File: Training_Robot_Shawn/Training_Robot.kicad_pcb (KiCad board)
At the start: 2 copper layers, 101.5 x 70 mm, 16 parts, among them J1 Arduino connector, J4 3V, J5 GND, M1 FrontL, M2 FrontR, M3 BackL, M4 BackR, SW1 SW_SPDT_312

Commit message: Update contstraints
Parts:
- moved G*** 7.50 mm to (233.0, 92.0)
- moved D1 5.39 mm to (211.0, 88.0)
- moved M1 5.39 mm to (194.5, 82.0)
- moved M2 5.39 mm to (194.5, 58.0)
- moved M3 5.39 mm to (195.5, 95.5)
- moved M4 5.39 mm to (195.5, 71.5)
- moved R1 5.39 mm to (215.4, 80.5)
- moved R2 5.39 mm to (211.0, 96.6)
- moved SW1 5.39 mm to (208.9, 80.5)
- moved U1 5.39 mm to (178.0, 61.8)
- moved U2 5.39 mm to (178.1, 85.6)
- moved U4 5.39 mm to (221.0, 65.5)
- moved J1 5.39 mm to (154.0, 68.0)
- moved J4 2.83 mm to (189.0, 47.5)
- moved J5 2.83 mm to (201.0, 47.5)
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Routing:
- net +3V3: track 176.0 -> 179.0 mm
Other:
- board size 101.5 x 70 mm -> 112.5 x 87 mm
- board text added: "Shawn Mitchell Thanks Jayrady Sok Josalin Wang Austen Yun Carlos Giron"
- board text removed: "Shawn Mitchell Thanks Jayrady Sok Josalin Wang"

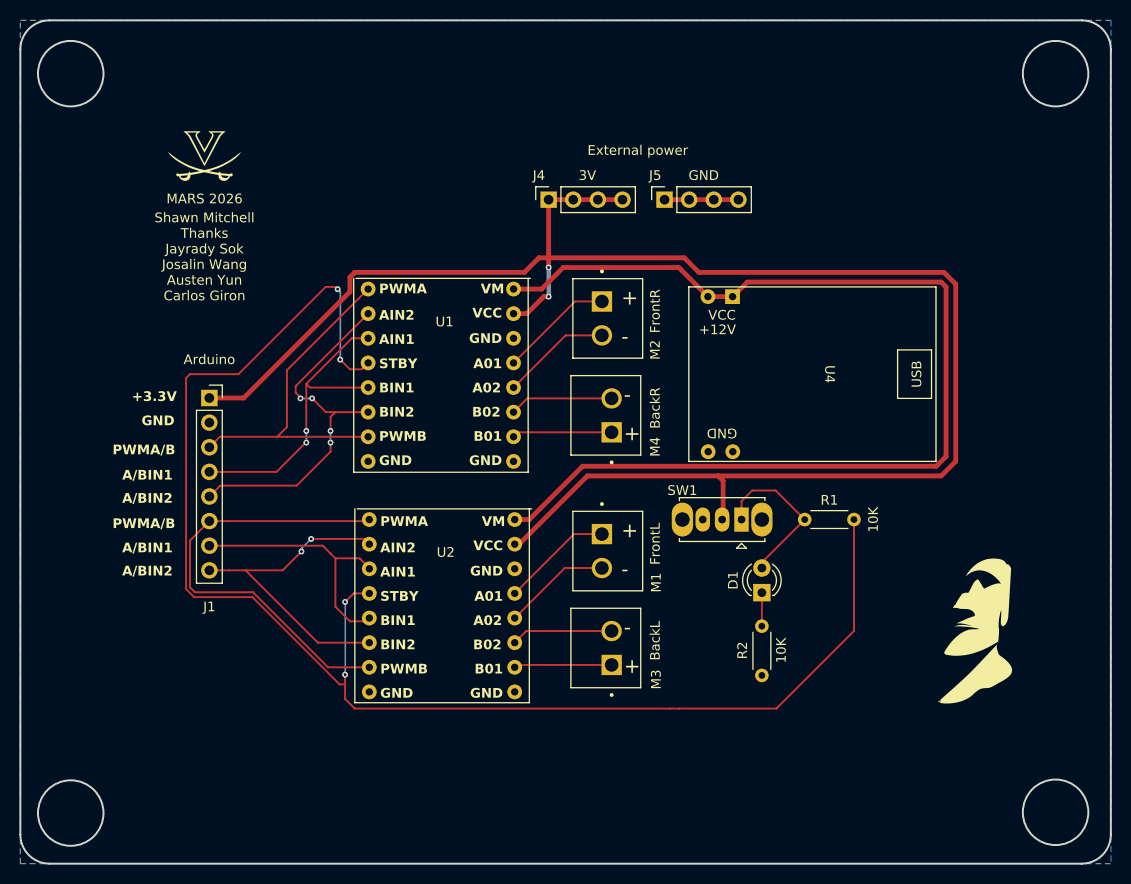
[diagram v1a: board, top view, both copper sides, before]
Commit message: moved a tiny bit
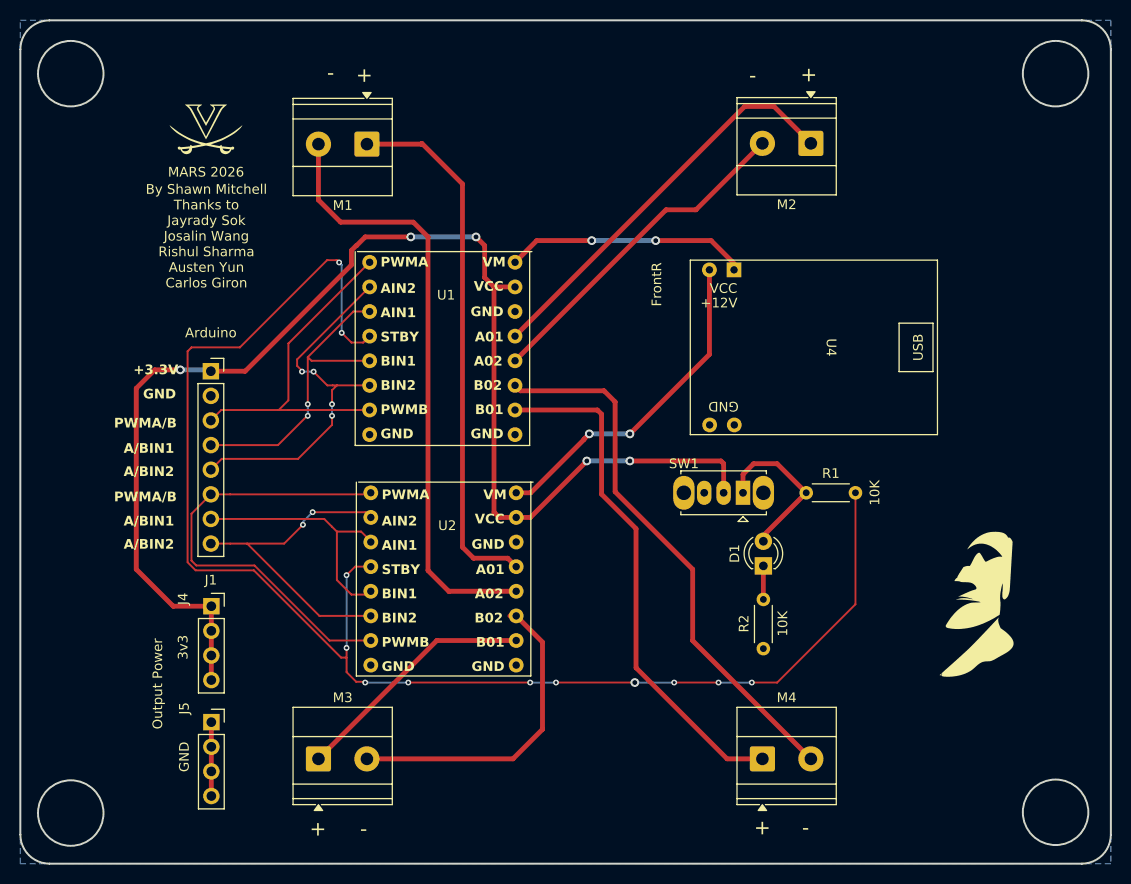
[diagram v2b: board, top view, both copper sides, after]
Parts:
- J4: value 3V -> 3v3
- M1, M2, M3, M4: footprint Library:CUI_TBP03R2-350-02BE -> TerminalBlock_Phoenix:TerminalBlock_Phoenix_MKDS-1,5-2_1x02_P5.00mm_Horizontal
- moved J5 71.4 mm to (154.2, 101.4), turned to 0 degrees
- moved J4 54.5 mm to (154.2, 89.4), turned to 0 degrees
- moved M1 47.0 mm to (170.3, 41.8), turned to 180 degrees
- moved M4 37.1 mm to (211.1, 105.2), turned to 0 degrees
- moved M3 31.8 mm to (165.3, 105.2), turned to 0 degrees
- moved M2 27.0 mm to (216.1, 41.7), turned to 180 degrees
- moved D1 2.77 mm to (211.2, 85.3)
- moved G*** 2.77 mm to (153.7, 40.2)
- moved U4 2.77 mm to (221.1, 62.7)
- moved R1 2.77 mm to (215.6, 77.7)
- moved G*** 2.77 mm to (233.2, 89.2)
- moved J1 2.77 mm to (154.2, 65.2)
- moved R2 2.77 mm to (211.2, 93.8)
- moved SW1 2.77 mm to (209.1, 77.7)
- moved U1 2.77 mm to (178.2, 59.0)
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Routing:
- net +12V motor pwr: track 112.3 -> 59.8 mm, vias 0 -> 4
- net /FL-: track 11.1 -> 63.1 mm
- net /BR-: track 10.7 -> 56.2 mm
- net /BR+: track 10.3 -> 54.3 mm
- net /FL+: track 11.5 -> 55.5 mm
- net +3V3: track 179.0 -> 139.5 mm, vias 2 -> 5
- net /FR+: track 11.7 -> 41.9 mm
- net /FR-: track 11.3 -> 34.8 mm
- net /BL-: track 10.5 -> 32.9 mm
- net /BL+: track 10.1 -> 25.8 mm
- net /STBY: track 153.4 -> 153.6 mm, vias 4 -> 12
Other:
- board text added: "By Shawn Mitchell Thanks to Jayrady Sok Josalin Wang Rishul Sharma Austen Yun Carlos Giron"
- board text added: "Output Power"
- board text removed: "External power"
- board text removed: "M2"
- board text removed: "M4"
- board text removed: "Shawn Mitchell Thanks Jayrady Sok Josalin Wang Austen Yun Carlos Giron"

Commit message: reduced size profile to 3x3 inches between mounting holes (horizontally and vertically)
reduced from 3x4 in between holes
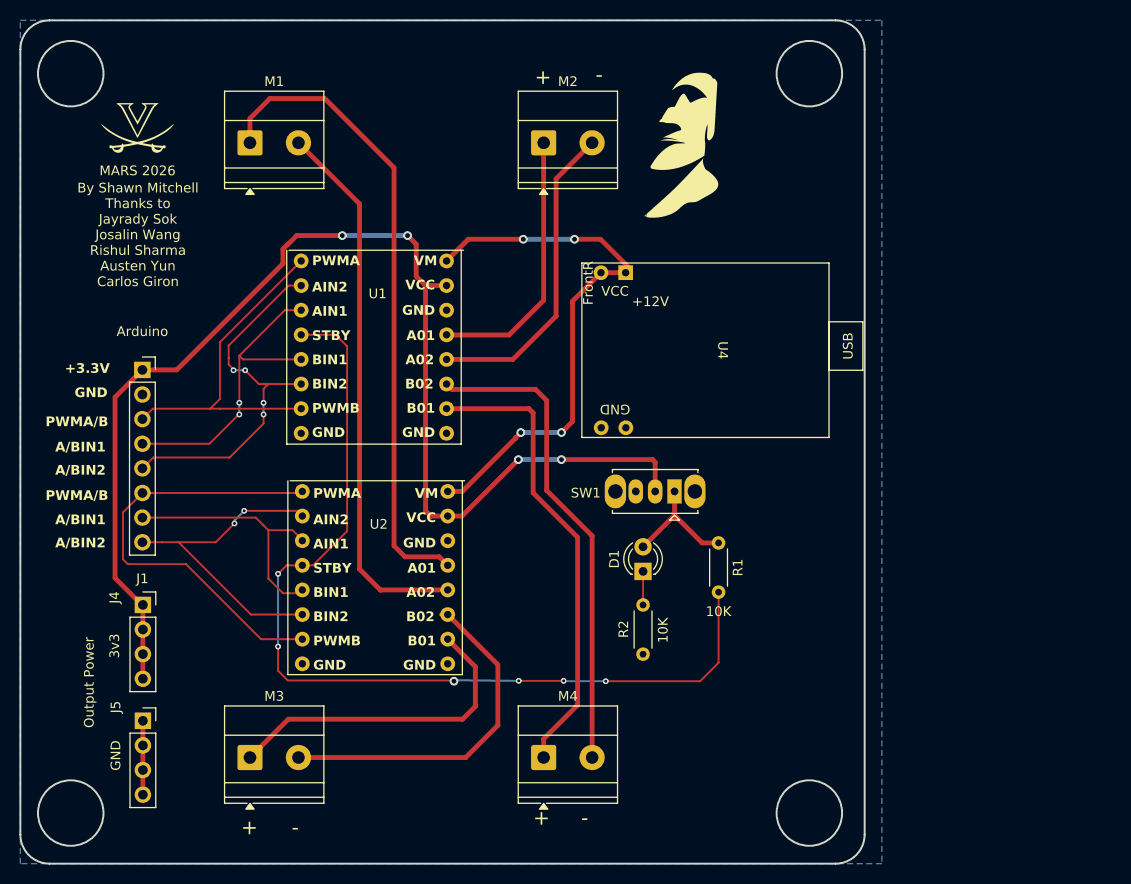
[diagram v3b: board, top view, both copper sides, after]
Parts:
- moved G*** 56.3 mm to (202.7, 41.9)
- moved M2 27.6 mm to (188.5, 41.6), turned to 0 degrees
- moved M4 22.6 mm to (188.5, 105.0)
- moved D1 12.4 mm to (198.7, 85.8)
- moved R2 12.4 mm to (198.7, 94.4)
- moved M1 12.1 mm to (158.2, 41.6), turned to 0 degrees
- moved U4 11.2 mm to (209.9, 63.0)
- moved R1 10.4 mm to (206.5, 82.9), turned to -90 degrees
- moved J4 7.06 mm to (147.1, 89.3)
- moved J5 7.06 mm to (147.1, 101.3)
- moved G*** 7.06 mm to (146.6, 40.1)
- moved J1 7.06 mm to (147.1, 65.1)
- moved M3 7.06 mm to (158.2, 105.0)
- moved SW1 7.06 mm to (202.0, 77.6)
- moved U1 7.06 mm to (171.1, 58.9)
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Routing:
- net /STBY: track 153.6 -> 97.3 mm, vias 12 -> 6
- net /FR+: track 41.9 -> 27.8 mm
- net /FL+: track 55.5 -> 66.5 mm
- net +3V3: track 139.5 -> 129.9 mm, vias 5 -> 4
- net /BL+: track 25.8 -> 33.9 mm
- net /BR-: track 56.2 -> 49.2 mm
- net /FL-: track 63.1 -> 56.6 mm
- net /BR+: track 54.3 -> 48.1 mm
- net Net-(D1-A): track 16.9 -> 12.8 mm
- net /BL-: track 32.9 -> 36.2 mm
- net +12V motor pwr: track 59.8 -> 56.7 mm
- net /FR-: track 34.8 -> 32.6 mm
- net Net-(J1-Pin_5): track 38.3 -> 39.1 mm
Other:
- board size 112.5 x 87 mm -> 87.1 x 87 mm
- board text removed: "M1"
- board text removed: "M3"

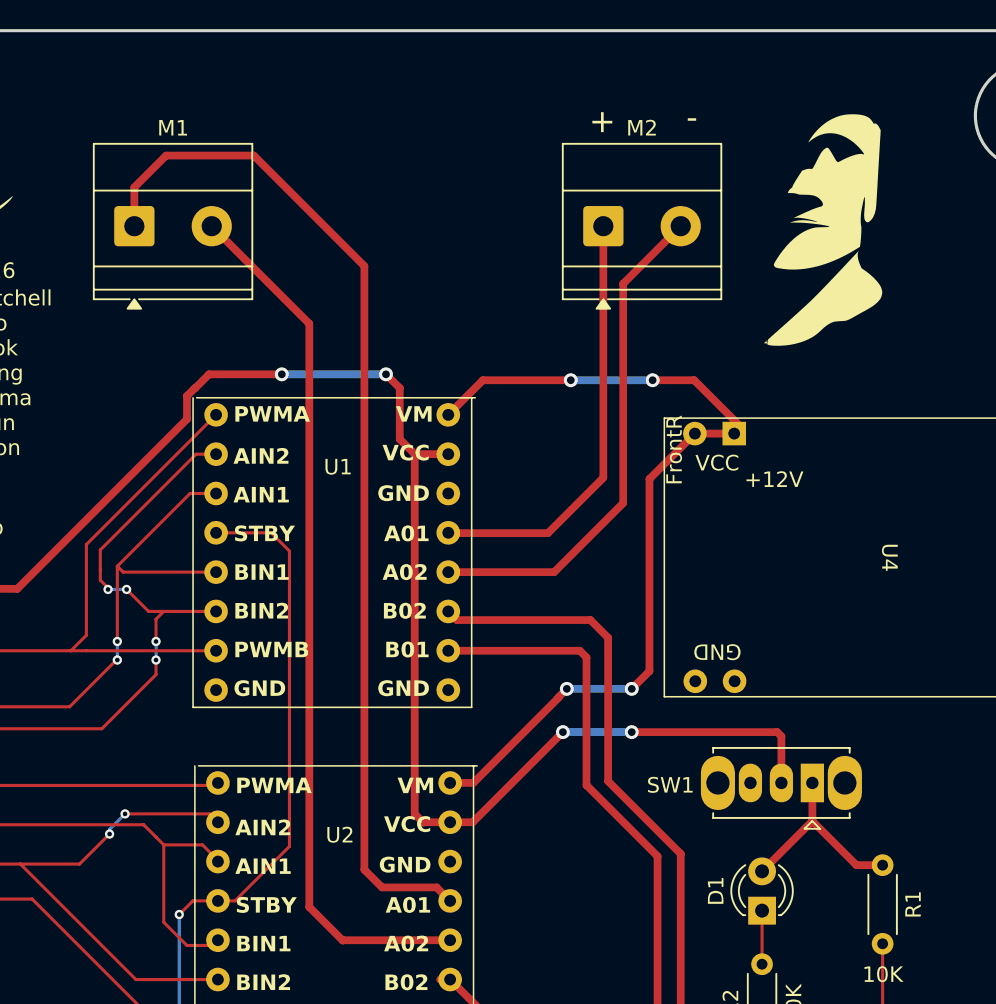
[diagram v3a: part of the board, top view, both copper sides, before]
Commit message: corrected direction of motor screw terminals
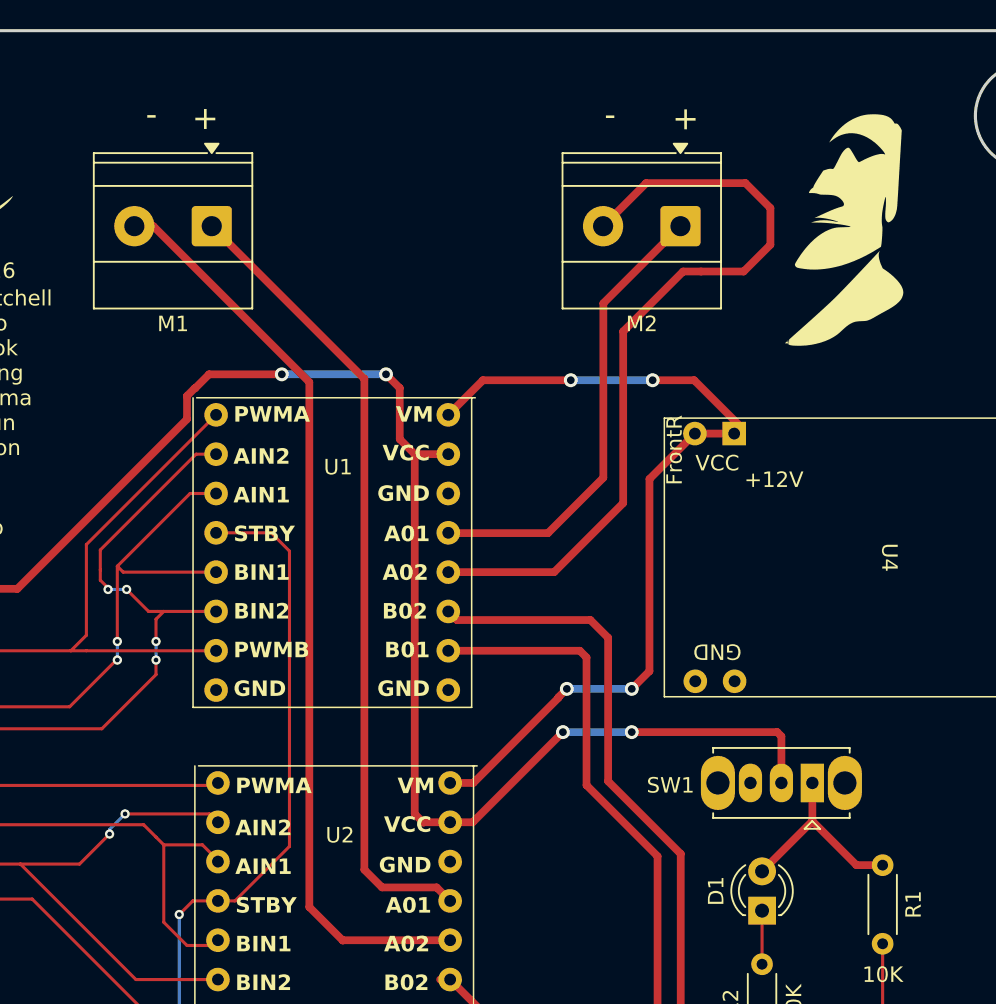
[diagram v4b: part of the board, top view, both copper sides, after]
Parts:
- moved M1 5.00 mm to (163.2, 41.6), turned to 180 degrees
- moved M2 4.98 mm to (193.5, 41.6), turned to 180 degrees
- moved G*** 1.36 mm to (204.1, 41.9)
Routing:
- net /FR-: track 32.6 -> 51.1 mm
- net /FL+: track 66.5 -> 52.0 mm
- net /FL-: track 56.6 -> 59.4 mm
- net /FR+: track 27.8 -> 29.8 mm

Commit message: added gerber files for final
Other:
- board text removed: "FrontR"
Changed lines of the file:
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@@
 			(drillshape 0)
 			(scaleselection 1)
-			(outputdirectory "Gerber/")
+			(outputdirectory "Gerber/Mar 8 gbr/")
 		)
 	)
@@
 		(property "Value" "FrontR"
 			(at 2.5 5.72 0)
-			(layer "F.Fab")
+			(layer "F.SilkS")
 			(effects
 				(font
@@
 		(attr through_hole)
 		(fp_line
-			(start -0.29 -1.236)
-			(end -0.29 -1.08)
+			(start -0.385259 -1.310958)
+			(end -0.385259 -1.21)
 			(stroke
 				(width 0.12)
@@
 		)
 		(fp_line
-			(start -0.29 1.08)
-			(end -0.29 1.236)
-			(stroke
-				(width 0.12)
-				(type solid)
-			)
-			(layer "F.SilkS")
-		)
-		(fp_arc
-			(start -0.29 -1.235516)
-			(mid 1.36566 -1.987699)
-			(end 2.941437 -1.08)
+			(start -0.34 1.16)
+			(end -0.34 1.270949)
 			(stroke
 				(width 0.12)
@@
 		)
 		(fp_arc
-			(start 0.229039 -1.08)
-			(mid 1.27 -1.5)
-			(end 2.310961 -1.08)
+			(start -0.385259 -1.31096)
+			(mid 1.371502 -2.109075)
+			(end 3.043501 -1.145947)
 			(stroke
 				(width 0.12)
@@
 		)
 		(fp_arc
-			(start 2.941437 1.08)
-			(mid 1.36566 1.987699)
-			(end -0.29 1.235516)
-			(stroke
-				(width 0.12)
-				(type solid)
-			)
-			(layer "F.SilkS")
-		)
-		(fp_arc
-			(start 2.310961 1.08)
-			(mid 1.27 1.5)
-			(end 0.229039 1.08)
+			(start 2.989371 1.110974)
+			(mid 1.368403 2.044705)
+			(end -0.33474 1.270949)
 			(stroke
 				(width 0.12)
@@
 		)
 		(property "Value" "BackR"
-			(at 2.5 5.72 0)
-			(layer "F.Fab")
+			(at 2.521 8.615 0)
+			(layer "F.SilkS")
 			(effects
 				(font
@@
 				(font
 					(size 1 1)
-					(thickness 0.15)
+					(thickness 0.2)
 				)
 			)
@@
 			(end -9 -8)
 			(stroke
-				(width 0.1)
-				(type default)
+				(width 0.2)
+				(type solid)
 			)
 			(layer "F.SilkS")
@@
 			(end -9 17.5)
 			(stroke
-				(width 0.1)
-				(type default)
+				(width 0.2)
+				(type solid)
 			)
 			(layer "F.SilkS")
@@
 			(end 9 -8)
 			(stroke
-				(width 0.1)
-				(type default)
+				(width 0.2)
+				(type solid)
 			)
 			(layer "F.SilkS")
@@
 			(end 9 17.5)
 			(stroke
-				(width 0.1)
-				(type default)
+				(width 0.2)
+				(type solid)
 			)
 			(layer "F.SilkS")
@@
 		)
 		(property "Value" "BackL"
-			(at 2.5 5.72 0)
-			(layer "F.Fab")
+			(at 2.465 8.869 0)
+			(layer "F.SilkS")
 			(effects
 				(font
@@
 		(property "Value" "FrontL"
 			(at 2.5 5.72 0)
-			(layer "F.Fab")
+			(layer "F.SilkS")
 			(effects
 				(font
@@
 		(attr through_hole)
 		(fp_line
-			(start -9.10969 13.817571)
-			(end -9.10969 -6.182429)
+			(start -9.10969 -6.182429)
+			(end 8.89031 -6.182429)
 			(stroke
-				(width 0.1)
-				(type default)
+				(width 0.2)
+				(type solid)
 			)
 			(layer "F.SilkS")
 		)
 		(fp_line
-			(start -8.874548 -6.182429)
-			(end 9.125452 -6.182429)
+			(start -9.10969 13.817571)
+			(end -9.10969 -6.182429)
 			(stroke
-				(width 0.1)
-				(type default)
+				(width 0.2)
+				(type solid)
 			)
 			(layer "F.SilkS")
@@
 			(end 8.89031 13.817571)
 			(stroke
-				(width 0.1)
-				(type default)
+				(width 0.2)
+				(type solid)
 			)
 			(layer "F.SilkS")
@@
 			(end -9.10969 13.817571)
 			(stroke
-				(width 0.1)
-				(type default)
+				(width 0.2)
+				(type solid)
 			)
 			(layer "F.SilkS")
@@
 		(attr through_hole)
 		(fp_line
-			(start -9.10969 13.817571)
-			(end -9.10969 -6.182429)
+			(start -9.10969 -6.182429)
+			(end 8.89031 -6.182429)
 			(stroke
-				(width 0.1)
-				(type default)
+				(width 0.2)
+				(type solid)
 			)
 			(layer "F.SilkS")
 		)
 		(fp_line
-			(start -8.874548 -6.182429)
-			(end 9.125452 -6.182429)
+			(start -9.10969 13.817571)
+			(end -9.10969 -6.182429)
 			(stroke
-				(width 0.1)
-				(type default)
+				(width 0.2)
+				(type solid)
 			)
 			(layer "F.SilkS")
@@
 			(end 8.89031 13.817571)
 			(stroke
-				(width 0.1)
-				(type default)
+				(width 0.2)
+				(type solid)
 			)
 			(layer "F.SilkS")
@@
 			(end -9.10969 13.817571)
 			(stroke
-				(width 0.1)
-				(type default)
+				(width 0.2)
+				(type solid)
 			)
 			(layer "F.SilkS")
@@
 	(gr_rect
 		(start 217.92 60.1)
-		(end 221.42 65.1)
+		(end 220.912 65.1)
 		(stroke
-			(width 0.1)
-			(type default)
+			(width 0.2)
+			(type solid)
 		)
 		(fill no)
@@
 		)
 	)
-	(gr_text "FrontR"
-		(at 193.09 56.1 90)
-		(layer "F.SilkS")
-		(effects
-			(font
-				(size 1 1)
-				(thickness 0.15)
-			)
-		)
-	)
